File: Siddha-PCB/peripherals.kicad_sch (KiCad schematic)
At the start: 4 parts, among them M1 Motor_Servo, M2 Motor_Servo

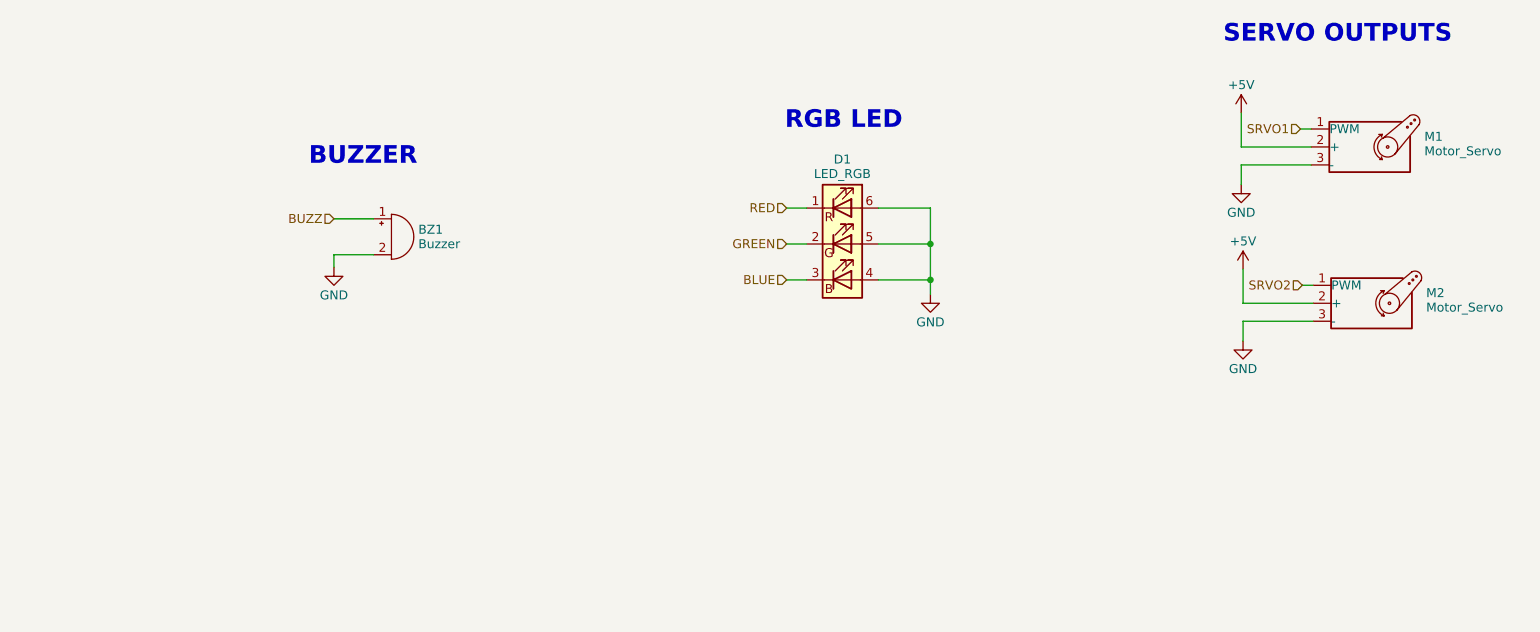
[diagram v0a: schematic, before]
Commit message: switch to linear actuator and 7.4v battery
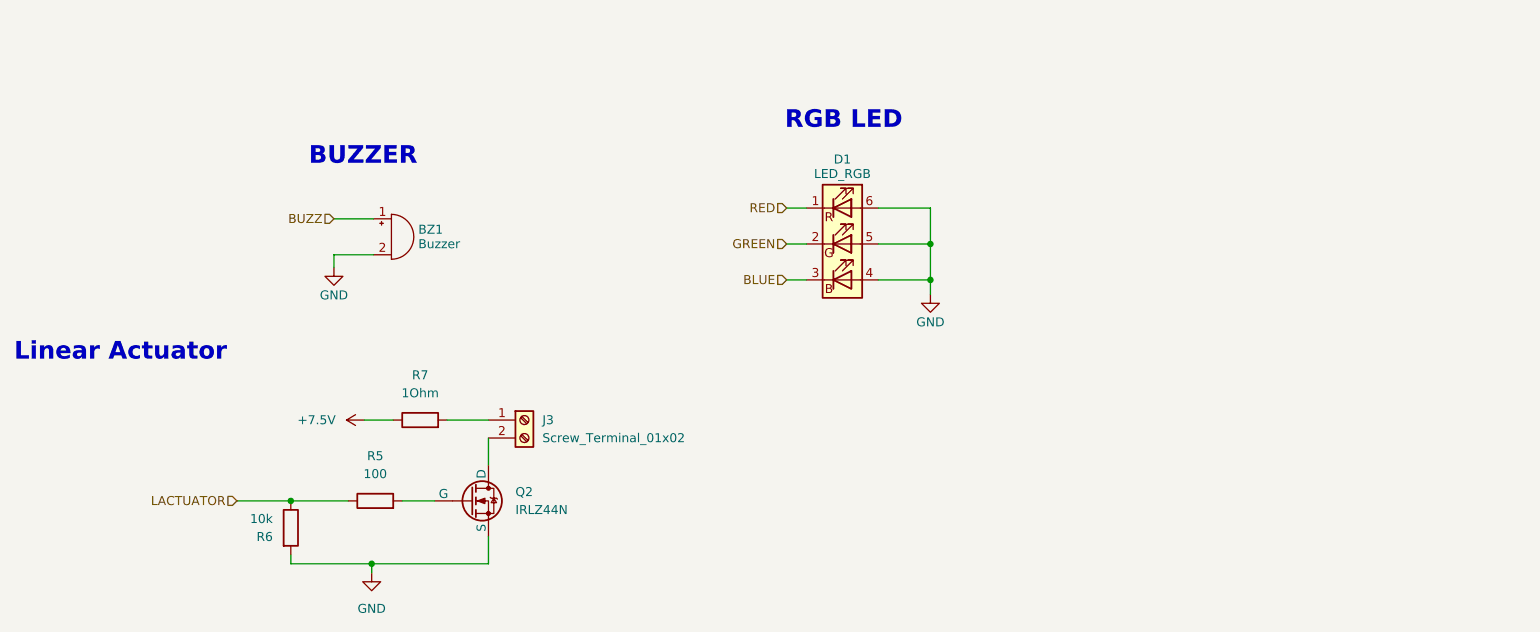
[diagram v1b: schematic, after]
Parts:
- removed M1, M2: Motor_Servo, symbol Motor:Motor_Servo
- added J3: Screw_Terminal_01x02, symbol Connector:Screw_Terminal_01x02
- added Q2: IRLZ44N, symbol Simulation_SPICE:NMOS
- added R5: 100, symbol Device:R
- added R6: 10k, symbol Device:R
- added R7: 1Ohm, symbol Device:R
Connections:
- net GND: now also Q2.3 (S), R6.2
- new net: J3.1 (Pin_1), R7.2
- new net: Q2.2 (G), R5.2
- new net: J3.2 (Pin_2), Q2.1 (D)
- new net +7.5V: R7.1
- new net LACTUATOR: R5.1, R6.1
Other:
- note added: "Linear Actuator"
- note removed: "SERVO OUTPUTS"
